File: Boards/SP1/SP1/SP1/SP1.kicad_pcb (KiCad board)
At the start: 2 copper layers, 49 x 49 mm, 31 parts, among them CON1 Micro_SD_Card, IC1 ATMEGA2560-A, J1 ISP, J2 DCJ0202, P1 CONN_01X04, P2 CONN_01X05, P3 CONN_01X03, U1 I2C-4PIN, U2 4050, U3 AP1117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

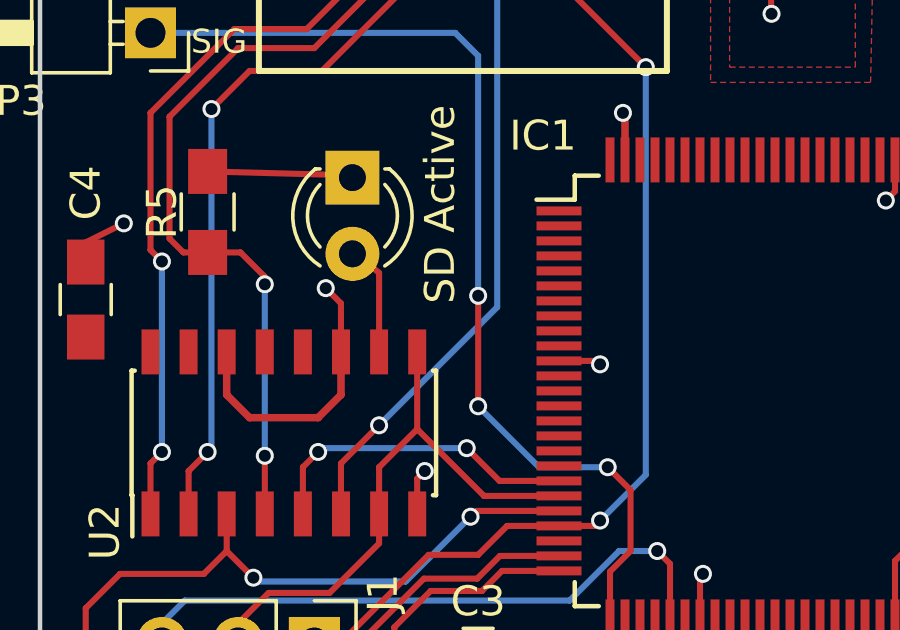
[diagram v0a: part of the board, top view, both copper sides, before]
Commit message: Built I2C Daisychain Card
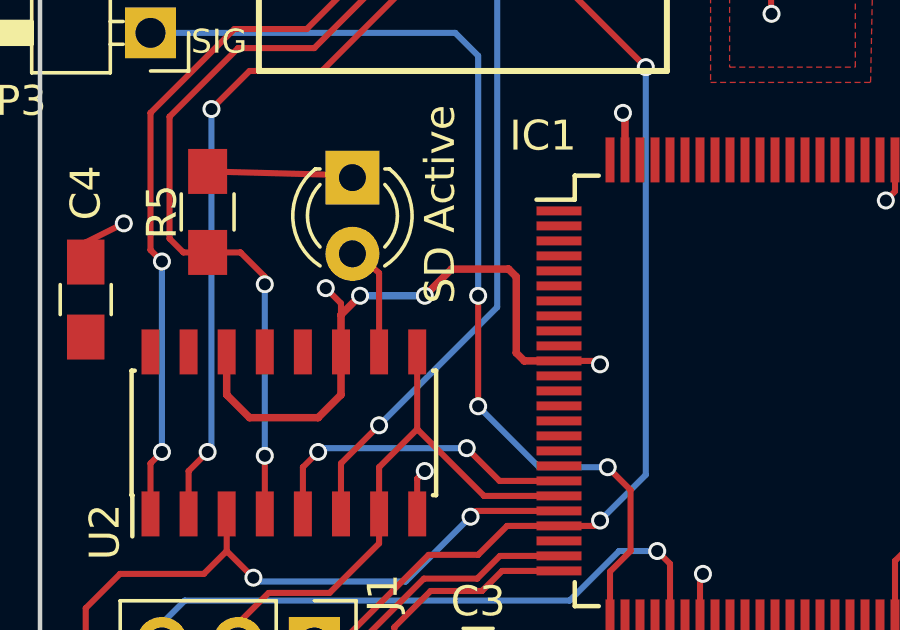
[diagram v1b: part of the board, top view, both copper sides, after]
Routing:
- net GND: track 43.7 -> 55.6 mm, vias 13 -> 15
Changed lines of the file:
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@@
   (general
     (links 83)
-    (no_connects 1)
+    (no_connects 0)
     (area -6.942001 -3.326001 55.383001 55.256001)
     (thickness 1.6)
     (drawings 21)
-    (tracks 293)
+    (tracks 304)
     (zones 0)
     (modules 31)
@@
   )
   (setup
-    (last_trace_width 0.2032)
+    (last_trace_width 0.25)
     (user_trace_width 0.2032)
     (user_trace_width 0.635)
@@
   (segment (start 34.417 38.354) (end 34.417 19.558) (width 0.2032) (layer B.Cu) (net 63))
   (segment (start 29.718 43.053) (end 34.417 38.354) (width 0.2032) (layer B.Cu) (net 63))
+  (segment (start 10.033 22.7) (end 10.033 21.463) (width 0.25) (layer F.Cu) (net 81) (status 400000))
+  (segment (start 16.142 23) (end 17.3 23) (width 0.25) (layer F.Cu) (net 81) (status 800000))
+  (segment (start 15.875 22.733) (end 16.142 23) (width 0.25) (layer F.Cu) (net 81))
+  (segment (start 15.875 20.193) (end 15.875 22.733) (width 0.25) (layer F.Cu) (net 81))
+  (segment (start 15.621 19.939) (end 15.875 20.193) (width 0.25) (layer F.Cu) (net 81))
+  (segment (start 13.716 19.939) (end 15.621 19.939) (width 0.25) (layer F.Cu) (net 81))
+  (segment (start 12.827 20.828) (end 13.716 19.939) (width 0.25) (layer F.Cu) (net 81))
+  (via (at 12.827 20.828) (size 0.6) (drill 0.4) (layers F.Cu B.Cu) (net 81))
+  (segment (start 10.668 20.828) (end 12.827 20.828) (width 0.25) (layer B.Cu) (net 81))
+  (via (at 10.668 20.828) (size 0.6) (drill 0.4) (layers F.Cu B.Cu) (net 81))
+  (segment (start 10.033 21.463) (end 10.668 20.828) (width 0.25) (layer F.Cu) (net 81))
   (segment (start 33.147 35.921) (end 32.278 35.921) (width 0.25) (layer F.Cu) (net 81))
   (via (at 31.496 36.703) (size 0.6) (drill 0.4) (layers F.Cu B.Cu) (net 81))
@@
   (segment (start 28.5 17.347) (end 28.194 17.653) (width 0.2032) (layer F.Cu) (net 81))
   (segment (start 17.3 23) (end 18.555 23) (width 0.2032) (layer F.Cu) (net 81))
+  (segment (start 18.555 23) (end 18.669 23.114) (width 0.2032) (layer F.Cu) (net 81))
   (via (at 18.669 23.114) (size 0.6) (drill 0.4) (layers F.Cu B.Cu) (net 81))
-  (segment (start 18.555 23) (end 18.669 23.114) (width 0.2032) (layer F.Cu) (net 81))
   (segment (start 22 31.7) (end 22 30.197) (width 0.2032) (layer F.Cu) (net 81))
   (via (at 22.098 30.099) (size 0.6) (drill 0.4) (layers F.Cu B.Cu) (net 81))
